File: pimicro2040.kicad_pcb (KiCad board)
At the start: 2 copper layers, 17.8 x 33.5 mm, 41 parts, among them J1 Left, J2 Right, J3 Bottom, SW1 RESET, SW2 BOOT, U1 RP2040, U2 W25Q32JWUUIQ, U3 TLV73333PDBVR, Y1 X322512MSB4SI

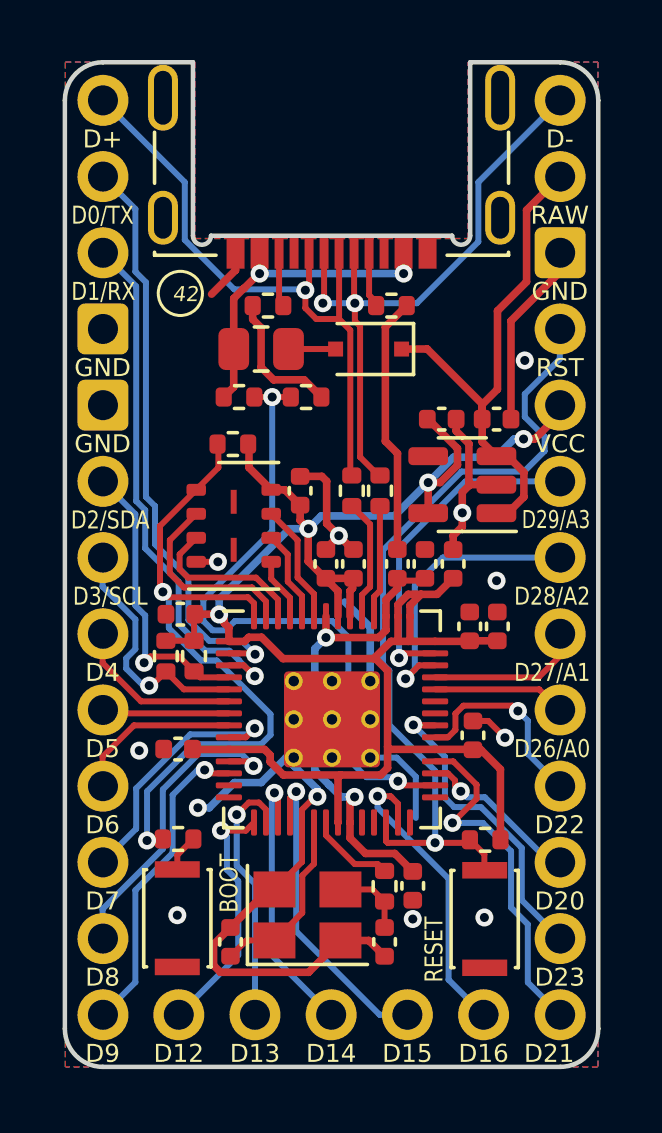
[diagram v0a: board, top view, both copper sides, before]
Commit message: Rev3 update
* Use HRO-TYPE-C-31-M-14
* Use 500 mA fuse instead of 350 mA one
* Improve layout (move USB termination resistors closer to MCU)
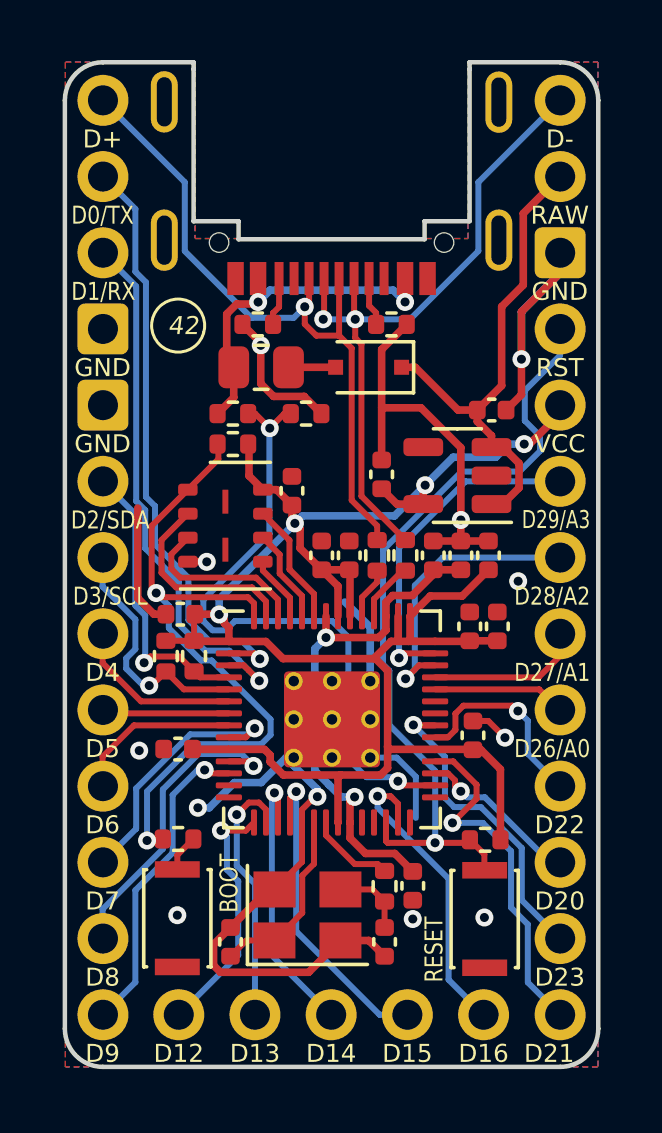
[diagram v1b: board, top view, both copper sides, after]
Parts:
- F1: value 350 mA -> 500 mA
- USB1: footprint 42keebs:Molex-216990_GCT-USB45xx_HRO-TYPE-C-31-M-13x-PiMicro -> 42keebs:TYPE-C-31-M-14-PiMicro
- moved C2 2.72 mm to (128.0, 68.7), turned to 90 degrees
- moved R3 2.31 mm to (128.8, 71.4)
- moved R4 2.31 mm to (127.8, 71.4)
- moved USB1 2.23 mm to (126.3, 57.2)
- moved C6 1.23 mm to (129.7, 71.4)
- moved C7 1.23 mm to (130.6, 71.4)
- moved C9 1.21 mm to (131.5, 71.4)
- moved R2 0.71 mm to (123.8, 63.7)
- moved R1 0.63 mm to (128.3, 63.7)
- moved D1 0.61 mm to (127.5, 65.2)
- moved F1 0.61 mm to (124.0, 65.2)
- moved R11 0.59 mm to (123.0, 66.7)
- moved R12 0.55 mm to (125.5, 66.7)
- moved C1 0.34 mm to (131.6, 66.6)
- moved U3 0.34 mm to (130.5, 68.8)
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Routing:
- net /D+: track 21.1 -> 23.5 mm
- net /USB_D+: track 4.04 -> 1.73 mm
- net /D-: track 21.1 -> 23.1 mm
- net /USB_D-: track 3.75 -> 2.01 mm
- net +1V1: track 15.9 -> 17.0 mm
- net VBUS: track 10.6 -> 11.6 mm
- net /RAW: track 17.6 -> 16.6 mm
- net +3V3: track 65.8 -> 64.9 mm
- net GND: track 58.4 -> 59.2 mm
- net Net-(U1-Pad30): track 22.3 -> 21.6 mm
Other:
- outline, holes or cut-outs redrawn
- board text added: "PiMicro2040 rev3 42Keebs.eu 2022"
- board text removed: "PiMicro2040 rev2 42Keebs.eu 2022"
